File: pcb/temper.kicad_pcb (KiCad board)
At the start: 6 copper layers, 164 x 234 mm, 168 parts, among them J1 ?, J2 ?, K1 ?, K2 ?, K3 ?, Q1 ?, Q2 ?, SW1 ?, SW2 ?, T1 ?, T2 ?, U1 ?, U10 ?, U11 ?, U12 ?, U13 ?, U14 ?, U15 ?, U16 ?, U17 ?, U18 ?, U19 ?, U2 ?, U20 ?, U21 ?, U22 ?, U23 ?, U24 ?, U25 ?, U26 ?, U27 ?, U3 ?, U4 ?, U5 ?, U6 ?, U7 ?, U8 ?, U9 ?

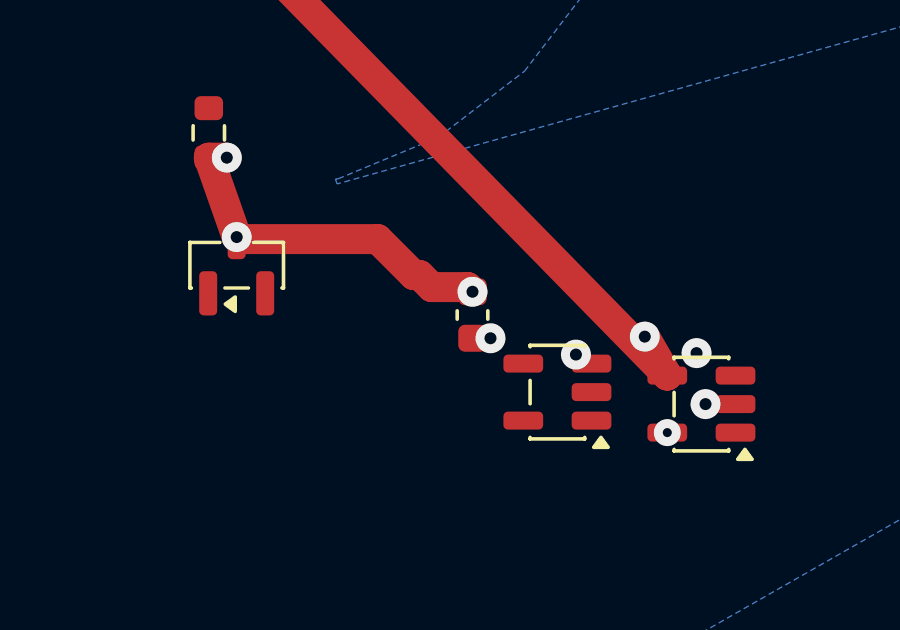
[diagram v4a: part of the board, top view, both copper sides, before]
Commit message: fix(pcb): move C16 1.50mm — closes the board's worst functional creepage gap
C16<->U14 measured 0.667mm against the 1.8mm FUNCTIONAL bar -- 37% of
required, by a wide margin the worst creepage gap of any class on this
board. Nothing else came under 1.2mm.

  C16 (30.06, 217.83) -> (28.56, 217.83)

  REQ-SAFE-01 total          62 -> 61
    creepage FUNCTIONAL 1.8mm 27 -> 26
  worst functional gap    0.667 -> 1.203mm  (37% -> 67% of required)

Every kicad-cli DRC category is UNCHANGED: errors 382, creepage 107,
courtyards_overlap 4, shorting_items 39, pth_inside_courtyard 0,
silk_over_copper 45, unconnected 347. The ceiling is untouched.

TARGET PICKED FROM THE DISTRIBUTION, not from the top of a list. The 27
functional violations are not 27 independent placement errors:

  C16<->U14   0.667mm   37% of required   <- the outlier
  U14<->U9    1.203mm   67%
  R53<->TP2   1.255mm   70%
  U19<->U3    1.470mm   82%
  C41<->U27   1.489mm   83%
  C11<->U15   1.500mm   83%
  D3 <->U17   1.500mm   83%
  R53<->U20   1.505mm   84%
  C15<->R62   1.505mm   84%
  C33<->U23   1.505mm   84%
  R45<->U8    1.505mm   84%
  R66<->U22   1.507mm   84%

Everything below the top two clusters hard at 1.489-1.507mm -- roughly
0.3mm short, all of it. That is the signature of a layout built to a ~1.5mm
functional-clearance convention that #1226 invalidated when it raised the
bar 1.0 -> 1.8mm, not of components individually mis-placed. Moving them
one at a time cannot fix a cluster like that; each needs ~0.3mm more,
everywhere at once. Only C16<->U14 is a genuine outlier, and that is what
this commit fixes.

U14 was searched first and rejected on measurement: 465 positions clear
BOTH its violations on the safety criteria, but all four DRC-scored
candidates blow up shorting_items 39 -> 45..48 and errors 382 -> 396..410.
U14 sits in dense copper. C16 -- the other half of the same pair -- has two
positions that are clean on every category, and this takes the nearer one.

  suite: 139 passed, 11 skip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
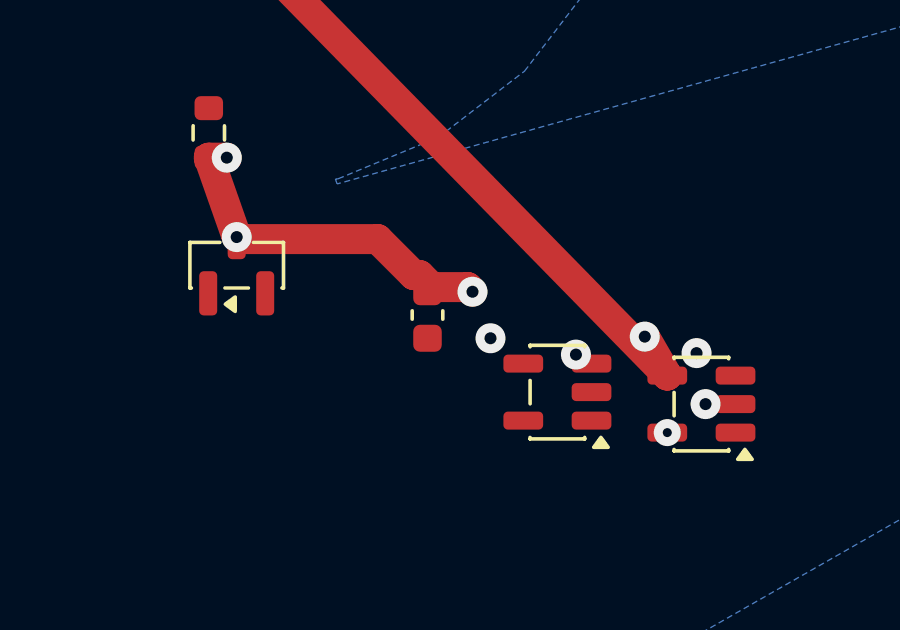
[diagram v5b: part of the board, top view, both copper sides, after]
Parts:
- moved C16 1.50 mm to (28.6, 217.8)
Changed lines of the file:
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@@
   )
   (footprint "Capacitor_SMD:C_0603_1608Metric" (version 20260206) (generator kicad-footprint-generator) (layer "F.Cu")
-    (at 30.06 217.83 90)
+    (at 28.56 217.83 90)
     (descr "Capacitor SMD 0603 (1608 Metric), square (rectangular) end terminal, IPC-7351 nominal, (Body size source: IPC-SM-782 page 76, https://www.pcb-3d.com/wordpress/wp-content/uploads/ipc-sm-782a_amendment_1_and_2.pdf)")
     (tags "capacitor")

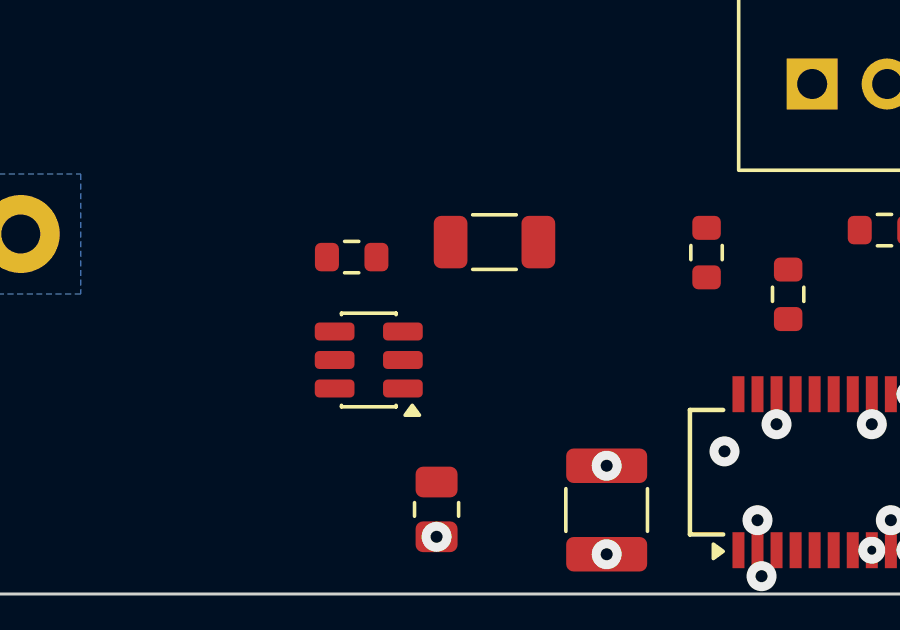
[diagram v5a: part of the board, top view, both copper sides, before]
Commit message: fix(pcb): move U21 and R48 clear of tank capacitor
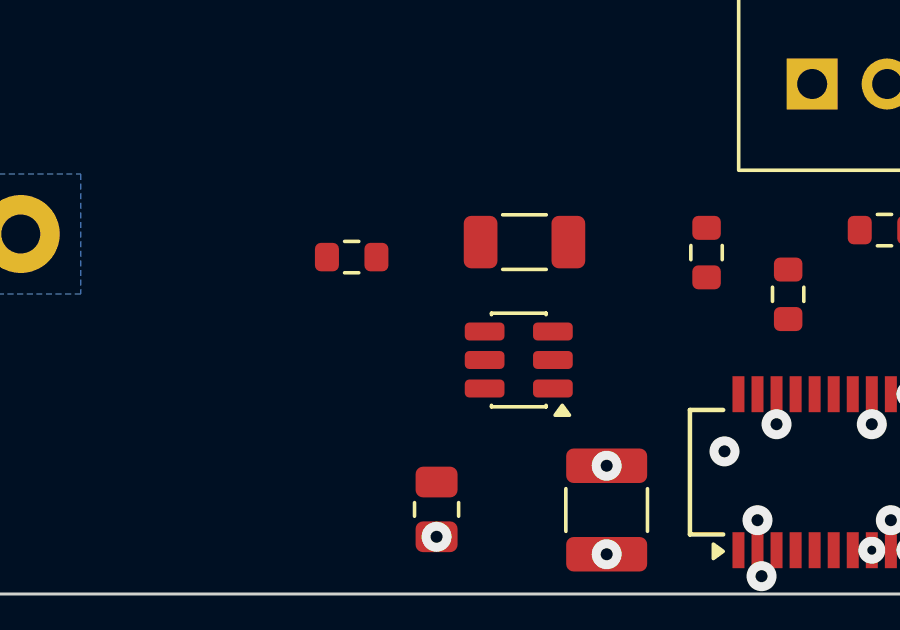
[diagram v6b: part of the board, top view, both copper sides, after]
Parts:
- moved U21 5.00 mm to (85.2, 246.2)
- moved R48 1.00 mm to (85.4, 242.3)
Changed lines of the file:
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@@
   )
   (footprint "Resistor_SMD:R_1206_3216Metric" (version 20260206) (generator kicad-footprint-generator) (layer "F.Cu")
-    (at 84.41 242.27 180)
+    (at 85.41 242.27 180)
     (descr "Resistor SMD 1206 (3216 Metric), square (rectangular) end terminal, IPC-7351 nominal, (Body size source: IPC-SM-782 page 72, https://www.pcb-3d.com/wordpress/wp-content/uploads/ipc-sm-782a_amendment_1_and_2.pdf)")
     (tags "resistor")
@@
   )
   (footprint "Package_TO_SOT_SMD:SOT-23-6" (version 20260206) (generator kicad-footprint-generator) (layer "F.Cu")
-    (at 80.22 246.2 180)
+    (at 85.22 246.2 180)
     (descr "SOT, 6 Pin (JEDEC MO-178 Var AB https://www.jedec.org/document_search?search_api_views_fulltext=MO-178)")
     (tags "SOT TO_SOT_SMD")

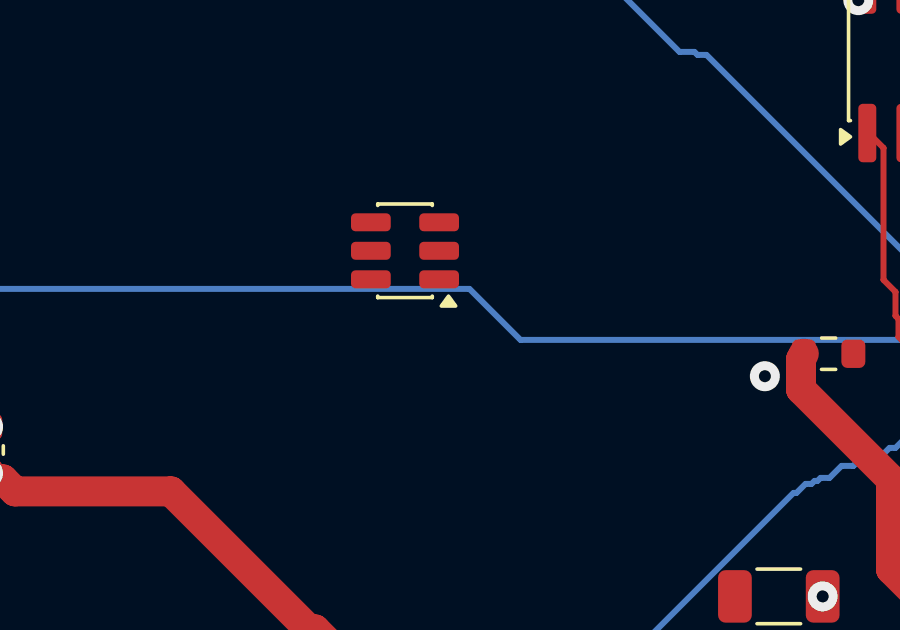
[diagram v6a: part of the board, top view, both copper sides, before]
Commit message: fix(pcb): move U13 clear of auxiliary input
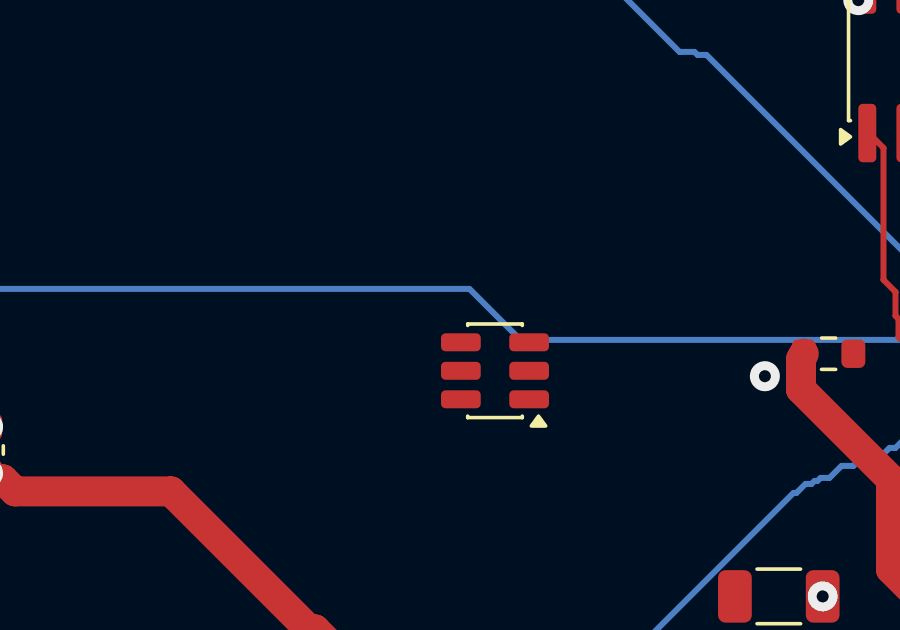
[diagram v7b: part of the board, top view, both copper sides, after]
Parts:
- moved U13 5.00 mm to (150.7, 46.5)
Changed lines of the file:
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@@
   )
   (footprint "Package_TO_SOT_SMD:SOT-23-6" (version 20260206) (generator kicad-footprint-generator) (layer "F.Cu")
-    (at 147.7 42.480000000000004 180)
+    (at 150.7 46.48 180)
     (descr "SOT, 6 Pin (JEDEC MO-178 Var AB https://www.jedec.org/document_search?search_api_views_fulltext=MO-178)")
     (tags "SOT TO_SOT_SMD")

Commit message: fix(pcb): relocate RTD fault pull-up to consumer
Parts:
- moved R43 17.6 mm to (27.0, 197.4)
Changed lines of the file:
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@@
   )
   (footprint "Resistor_SMD:R_0603_1608Metric" (version 20260206) (generator kicad-footprint-generator) (layer "F.Cu")
-    (at 41.54 187.57 180)
+    (at 27 197.4 180)
     (descr "Resistor SMD 0603 (1608 Metric), square (rectangular) end terminal, IPC-7351 nominal, (Body size source: IPC-SM-782 page 72, https://www.pcb-3d.com/wordpress/wp-content/uploads/ipc-sm-782a_amendment_1_and_2.pdf)")
     (tags "resistor")
